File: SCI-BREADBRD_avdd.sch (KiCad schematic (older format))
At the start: 25 parts, among them P8 TP, U2 TPS62240DDC, U3 TPS73401DDC, U4 TS5A3159ADCK, U5 TS5A3159ADCK

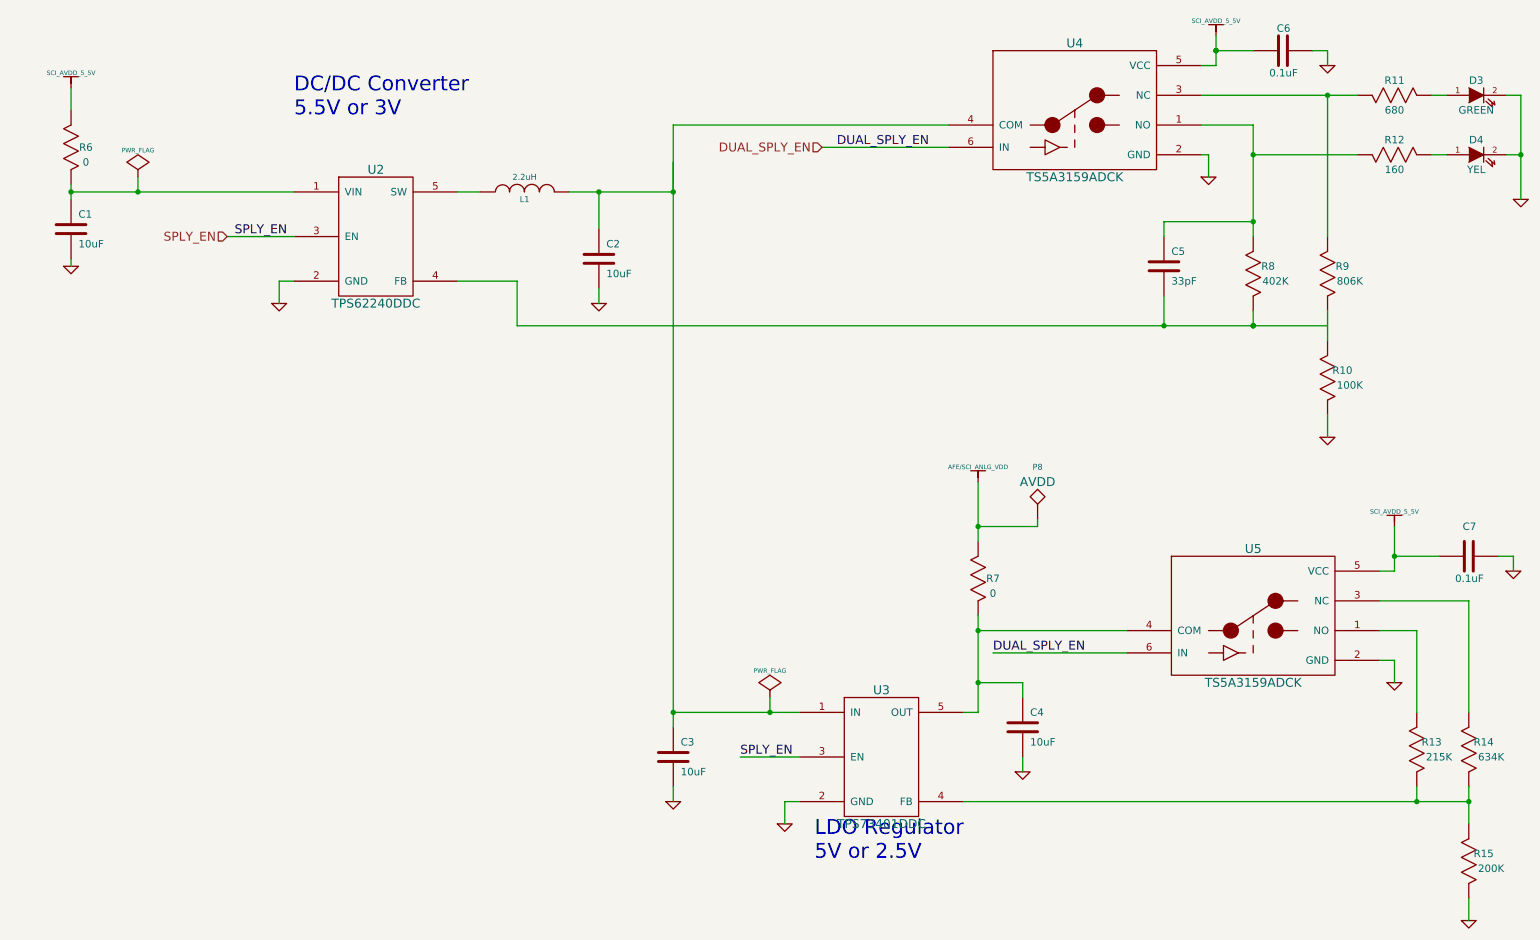
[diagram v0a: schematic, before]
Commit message: Enlarged the text on all of the power rails to make them easier to see when plotted
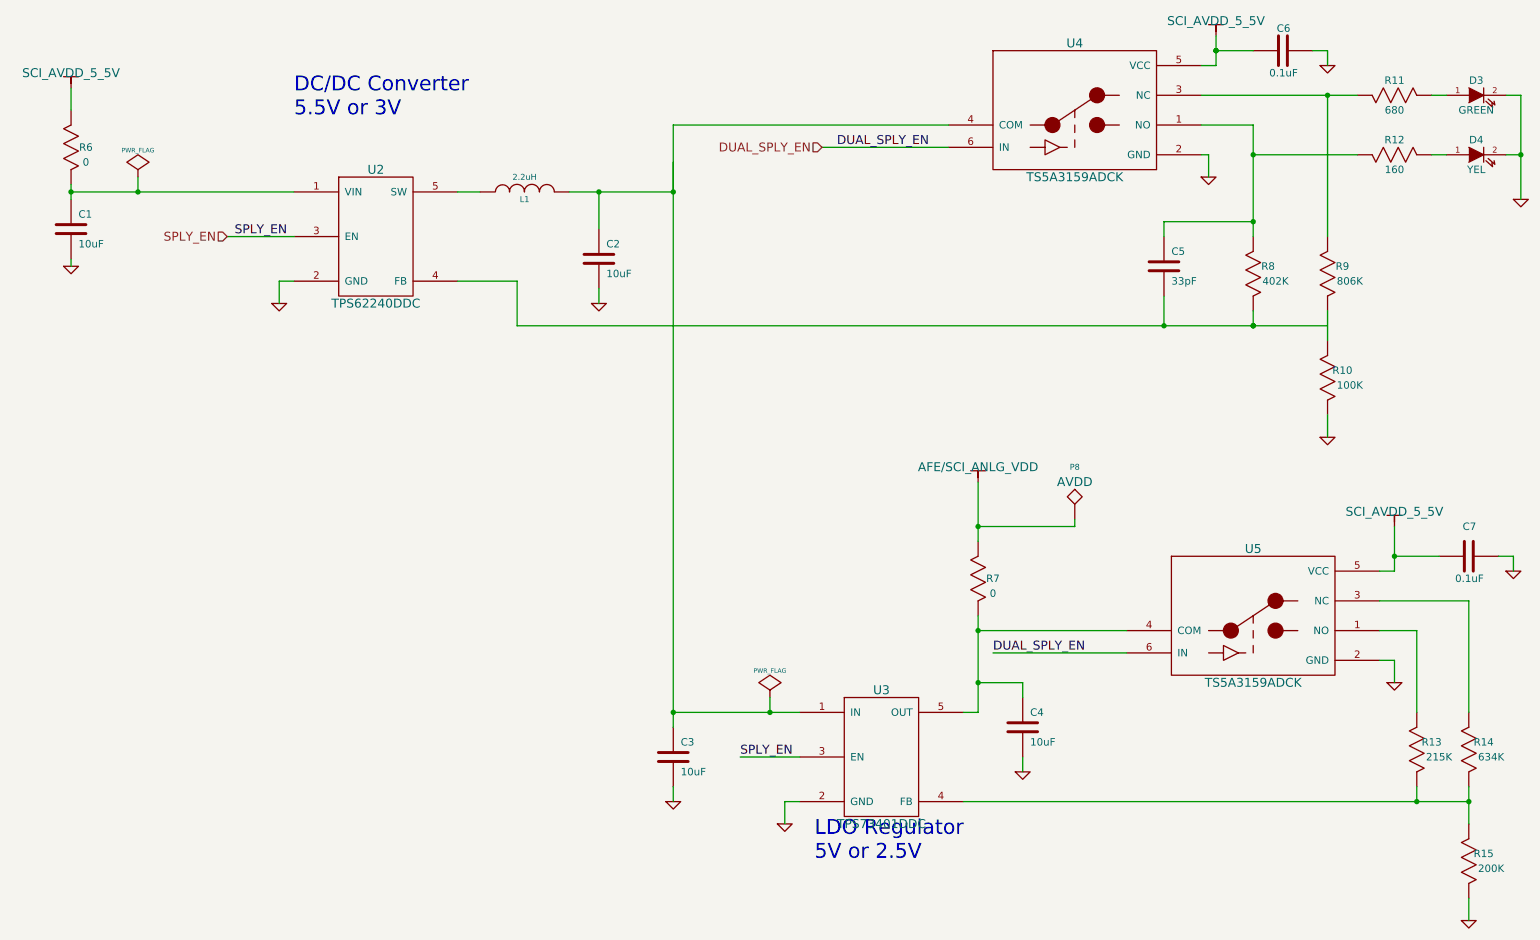
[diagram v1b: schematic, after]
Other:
- moved on the sheet: P8
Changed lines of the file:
@@
-EESchema Schematic File Version 2  date Fri 27 Apr 2012 01:46:56 PM EDT
+EESchema Schematic File Version 2  date Fri 27 Apr 2012 02:46:40 PM EDT
 LIBS:custom_transistors
 LIBS:TI_custom
@@
 $EndComp
 $Comp
-L SCI_AVDD_5_5V #PWR48
-U 1 1 4F9A30C2
-P 1000 1150
-F 0 "#PWR48" H 1000 1250 30  0001 C CNN
-F 1 "SCI_AVDD_5_5V" H 1000 1250 30  0000 C CNN
-	1    1000 1150
-	1    0    0    -1
-$EndComp
-$Comp
 L GND #PWR50
 U 1 1 4F9A30C8
@@
 $EndComp
 $Comp
-L SCI_AVDD_5_5V #PWR57
-U 1 1 4F9A3131
-P 8700 800
-F 0 "#PWR57" H 8700 900 30  0001 C CNN
-F 1 "SCI_AVDD_5_5V" H 8700 900 30  0000 C CNN
-	1    8700 800
-	1    0    0    -1
-$EndComp
-$Comp
 L C C5
 U 1 1 4F9A313A
@@
 $EndComp
 $Comp
-L SCI_AVDD_5_5V #PWR60
-U 1 1 4F9A3161
-P 9900 4100
-F 0 "#PWR60" H 9900 4200 30  0001 C CNN
-F 1 "SCI_AVDD_5_5V" H 9900 4200 30  0000 C CNN
-	1    9900 4100
-	1    0    0    -1
-$EndComp
-$Comp
 L GND #PWR61
 U 1 1 4F9A3167
@@
 	1    7100 4450
 	0    -1   -1   0
-$EndComp
-$Comp
-L AFE/SCI_ANLG_VDD #PWR54
-U 1 1 4F9A31AB
-P 7100 3800
-F 0 "#PWR54" H 7100 3900 30  0001 C CNN
-F 1 "AFE/SCI_ANLG_VDD" H 7100 3900 30  0000 C CNN
-	1    7100 3800
-	1    0    0    -1
 $EndComp
 Text Label 7200 4950 0    60   ~ 0
@@
 	1    0    0    -1
 $EndComp
+$Comp
+L TP P8
+U 1 1 4F9AD783
+P 7750 4050
+F 0 "P8" H 7750 4400 40  0000 C CNN
+F 1 "TP" H 7750 4300 30  0001 C CNN
+F 2 "TESTVIA_p30mil_h20mil" H 7750 4050 60  0001 C CNN
+F 4 "TESTPOINT VIA" H 7750 4050 60  0001 C CNN "Description"
+F 5 "NO PART. TEST PAD ONLY." H 7750 4050 60  0001 C CNN "Note"
+F 6 "AVDD" H 7750 4300 60  0000 C CNN "Silkscreen"
+	1    7750 4050
+	1    0    0    -1
+$EndComp
+$Comp
+L SCI_AVDD_5_5V #PWR?
+U 1 1 4F9AEF89
+P 1000 1150
+F 0 "#PWR?" H 1000 1250 30  0001 C CNN
+F 1 "SCI_AVDD_5_5V" H 1000 1250 60  0000 C CNN
+	1    1000 1150
+	1    0    0    -1
+$EndComp
+$Comp
+L SCI_AVDD_5_5V #PWR?
+U 1 1 4F9AEF98
+P 8700 800
+F 0 "#PWR?" H 8700 900 30  0001 C CNN
+F 1 "SCI_AVDD_5_5V" H 8700 900 60  0000 C CNN
+	1    8700 800
+	1    0    0    -1
+$EndComp
+$Comp
+L SCI_AVDD_5_5V #PWR?
+U 1 1 4F9AEFA7
+P 9900 4100
+F 0 "#PWR?" H 9900 4200 30  0001 C CNN
+F 1 "SCI_AVDD_5_5V" H 9900 4200 60  0000 C CNN
+	1    9900 4100
+	1    0    0    -1
+$EndComp
+$Comp
+L AFE/SCI_ANLG_VDD #PWR?
+U 1 1 4F9AEFC0
+P 7100 3800
+F 0 "#PWR?" H 7100 3900 30  0001 C CNN
+F 1 "AFE/SCI_ANLG_VDD" H 7100 3900 60  0000 C CNN
+	1    7100 3800
+	1    0    0    -1
+$EndComp
 Wire Wire Line
 	1000 1150 1000 1300
 Wire Wire Line
-	1000 1850 1450 1850
-Wire Wire Line
-	1450 1850 2500 1850
+	1000 1850 2500 1850
 Wire Wire Line
 	2400 2600 2400 2450
@@
 	2400 2450 2500 2450
 Wire Wire Line
-	1000 1800 1000 1850
-Wire Wire Line
-	1000 1850 1000 1900
+	1000 1800 1000 1900
 Connection ~ 1000 1850
 Wire Wire Line
@@
 	3600 1850 3750 1850
 Wire Wire Line
-	4350 1850 4550 1850
-Wire Wire Line
-	4550 1850 5050 1850
+	4350 1850 5050 1850
 Wire Wire Line
 	4550 2600 4550 2500
@@
 	8600 1400 8950 1400
 Wire Wire Line
-	8950 1400 8950 1600
-Wire Wire Line
-	8950 1600 8950 2050
-Wire Wire Line
-	8950 2050 8950 2150
+	8950 1400 8950 2150
 Wire Wire Line
 	8650 1600 8650 1750
@@
 	8650 1600 8600 1600
 Wire Wire Line
-	8600 1200 9450 1200
-Wire Wire Line
-	9450 1200 9650 1200
+	8600 1200 9650 1200
 Wire Wire Line
 	9450 2650 9450 2850
 Wire Wire Line
-	4000 2750 8350 2750
-Wire Wire Line
-	8350 2750 8950 2750
-Wire Wire Line
-	8950 2750 9450 2750
+	4000 2750 9450 2750
 Connection ~ 8950 2750
 Connection ~ 8950 2750
@@
 	4000 2450 3600 2450
 Wire Wire Line
-	8700 800  8700 900
-Wire Wire Line
-	8700 900  8700 1000
+	8700 800  8700 1000
 Wire Wire Line
 	8700 1000 8600 1000
@@
 	7100 5350 7000 5350
 Wire Wire Line
-	7100 4700 7100 4800
-Wire Wire Line
-	7100 4800 7100 5150
-Wire Wire Line
-	7100 5150 7100 5350
+	7100 4700 7100 5350
 Wire Wire Line
 	9900 5000 9800 5000
@@
 	10050 4800 9800 4800
 Wire Wire Line
-	10400 5850 10400 5950
-Wire Wire Line
-	10400 5950 10400 6100
+	10400 5850 10400 6100
 Wire Wire Line
 	10050 5850 10050 5950
 Wire Wire Line
-	7000 5950 10050 5950
-Wire Wire Line
-	10050 5950 10400 5950
+	7000 5950 10400 5950
 Connection ~ 10400 5950
 Connection ~ 10050 5950
@@
 	5050 5950 5050 5850
 Wire Wire Line
-	7100 3800 7100 4100
-Wire Wire Line
-	7100 4100 7100 4200
-Wire Wire Line
-	7100 4100 7500 4100
-Wire Wire Line
-	7500 4100 7500 4050
+	7100 3800 7100 4200
+Wire Wire Line
+	7100 4100 7750 4100
+Wire Wire Line
+	7750 4100 7750 4050
 Connection ~ 7100 4100
 Wire Wire Line
@@
 	6050 1550 6900 1550
 Wire Wire Line
-	5050 1400 5050 1850
-Wire Wire Line
-	5050 1650 5050 5350
-Wire Wire Line
-	5050 5350 5050 5450
+	5050 1850 5050 1400
+Wire Wire Line
+	5050 1650 5050 5450
 Wire Wire Line
 	4550 2100 4550 1850
 Connection ~ 4550 1850
 Wire Wire Line
-	5050 5350 5700 5350
-Wire Wire Line
-	5700 5350 5900 5350
+	5050 5350 5900 5350
 Connection ~ 5050 1850
 Connection ~ 5050 5350
@@
 Connection ~ 8950 1600
 Wire Wire Line
-	10750 1200 10750 1600
-Wire Wire Line
-	10750 1600 10750 1900
+	10750 1200 10750 1900
 Connection ~ 10750 1600
 Wire Wire Line
@@
 	10700 4300 10700 4400
 Wire Wire Line
-	9900 4100 9900 4300
-Wire Wire Line
-	9900 4300 9900 4400
+	9900 4100 9900 4400
 Wire Wire Line
 	9900 4400 9800 4400
@@
 	1450 1750 1450 1850
 Connection ~ 1450 1850
-$Comp
-L TP P8
-U 1 1 4F9AD783
-P 7500 4050
-F 0 "P8" H 7500 4400 40  0000 C CNN
-F 1 "TP" H 7500 4300 30  0001 C CNN
-F 2 "TESTVIA_p30mil_h20mil" H 7500 4050 60  0001 C CNN
-F 4 "TESTPOINT VIA" H 7500 4050 60  0001 C CNN "Description"
-F 5 "NO PART. TEST PAD ONLY." H 7500 4050 60  0001 C CNN "Note"
-F 6 "AVDD" H 7500 4300 60  0000 C CNN "Silkscreen"
-	1    7500 4050
-	1    0    0    -1
-$EndComp
 $EndSCHEMATC

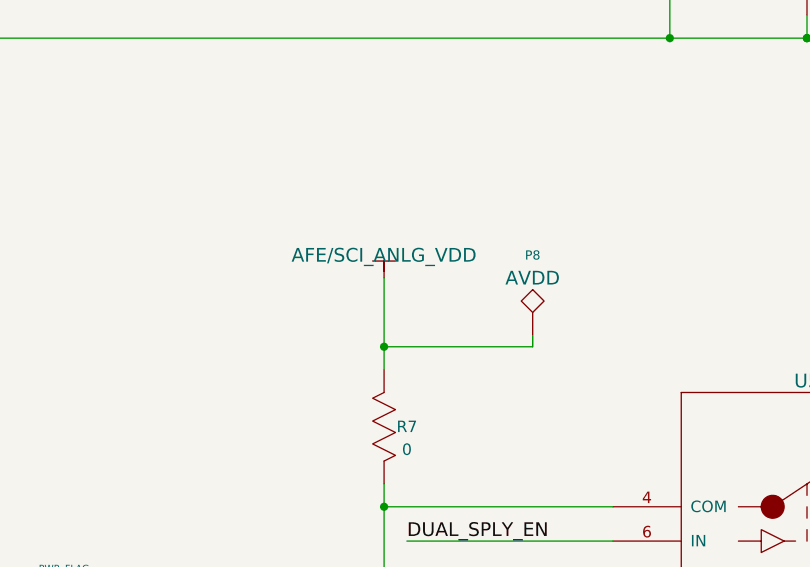
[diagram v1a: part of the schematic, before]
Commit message: No longer connecting the power circuitry directly to AFE/SCI_ANLG power rails.
This is just too dangerous with AFE modules that also generate power
on those rails. For this board, the user can manually jumper the
circuitry to the rails as desired.
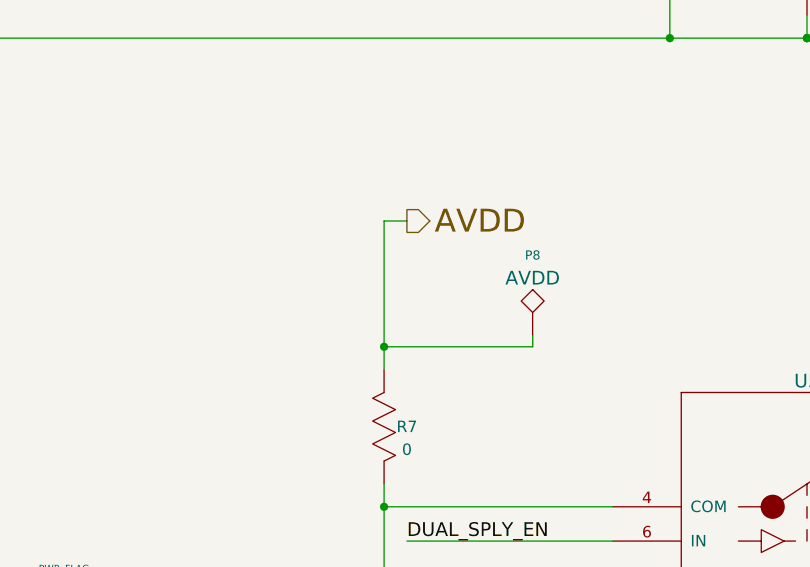
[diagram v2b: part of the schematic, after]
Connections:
- net AFE/SCI_ANLG_VDD renamed AVDD
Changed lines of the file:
@@
-EESchema Schematic File Version 2  date Fri 27 Apr 2012 02:46:40 PM EDT
+EESchema Schematic File Version 2  date Tue 01 May 2012 11:50:12 PM EDT
 LIBS:custom_transistors
 LIBS:TI_custom
@@
 Sheet 7 9
 Title "SCI-BREADBRD-MVK"
-Date "27 apr 2012"
+Date "2 may 2012"
 Rev "A"
 Comp "The Ohio State University"
@@
 $EndComp
 $Comp
+L SCI_AVDD_5_5V #PWR?
+U 1 1 4F9AEF89
+P 1000 1150
+F 0 "#PWR?" H 1000 1250 30  0001 C CNN
+F 1 "SCI_AVDD_5_5V" H 1000 1250 60  0000 C CNN
+	1    1000 1150
+	1    0    0    -1
+$EndComp
+$Comp
+L SCI_AVDD_5_5V #PWR?
+U 1 1 4F9AEF98
+P 8700 800
+F 0 "#PWR?" H 8700 900 30  0001 C CNN
+F 1 "SCI_AVDD_5_5V" H 8700 900 60  0000 C CNN
+	1    8700 800
+	1    0    0    -1
+$EndComp
+$Comp
+L SCI_AVDD_5_5V #PWR?
+U 1 1 4F9AEFA7
+P 9900 4100
+F 0 "#PWR?" H 9900 4200 30  0001 C CNN
+F 1 "SCI_AVDD_5_5V" H 9900 4200 60  0000 C CNN
+	1    9900 4100
+	1    0    0    -1
+$EndComp
+$Comp
 L TP P8
 U 1 1 4F9AD783
@@
 	1    0    0    -1
 $EndComp
-$Comp
-L SCI_AVDD_5_5V #PWR?
-U 1 1 4F9AEF89
-P 1000 1150
-F 0 "#PWR?" H 1000 1250 30  0001 C CNN
-F 1 "SCI_AVDD_5_5V" H 1000 1250 60  0000 C CNN
-	1    1000 1150
-	1    0    0    -1
-$EndComp
-$Comp
-L SCI_AVDD_5_5V #PWR?
-U 1 1 4F9AEF98
-P 8700 800
-F 0 "#PWR?" H 8700 900 30  0001 C CNN
-F 1 "SCI_AVDD_5_5V" H 8700 900 60  0000 C CNN
-	1    8700 800
-	1    0    0    -1
-$EndComp
-$Comp
-L SCI_AVDD_5_5V #PWR?
-U 1 1 4F9AEFA7
-P 9900 4100
-F 0 "#PWR?" H 9900 4200 30  0001 C CNN
-F 1 "SCI_AVDD_5_5V" H 9900 4200 60  0000 C CNN
-	1    9900 4100
-	1    0    0    -1
-$EndComp
-$Comp
-L AFE/SCI_ANLG_VDD #PWR?
-U 1 1 4F9AEFC0
-P 7100 3800
-F 0 "#PWR?" H 7100 3900 30  0001 C CNN
-F 1 "AFE/SCI_ANLG_VDD" H 7100 3900 60  0000 C CNN
-	1    7100 3800
-	1    0    0    -1
-$EndComp
+Text HLabel 7200 3550 2    100  Output ~ 0
+AVDD
 Wire Wire Line
 	1000 1150 1000 1300
@@
 	5050 5950 5050 5850
 Wire Wire Line
-	7100 3800 7100 4200
+	7100 3550 7100 4200
 Wire Wire Line
 	7100 4100 7750 4100
@@
 	1450 1750 1450 1850
 Connection ~ 1450 1850
+Wire Wire Line
+	7100 3550 7200 3550
 $EndSCHEMATC

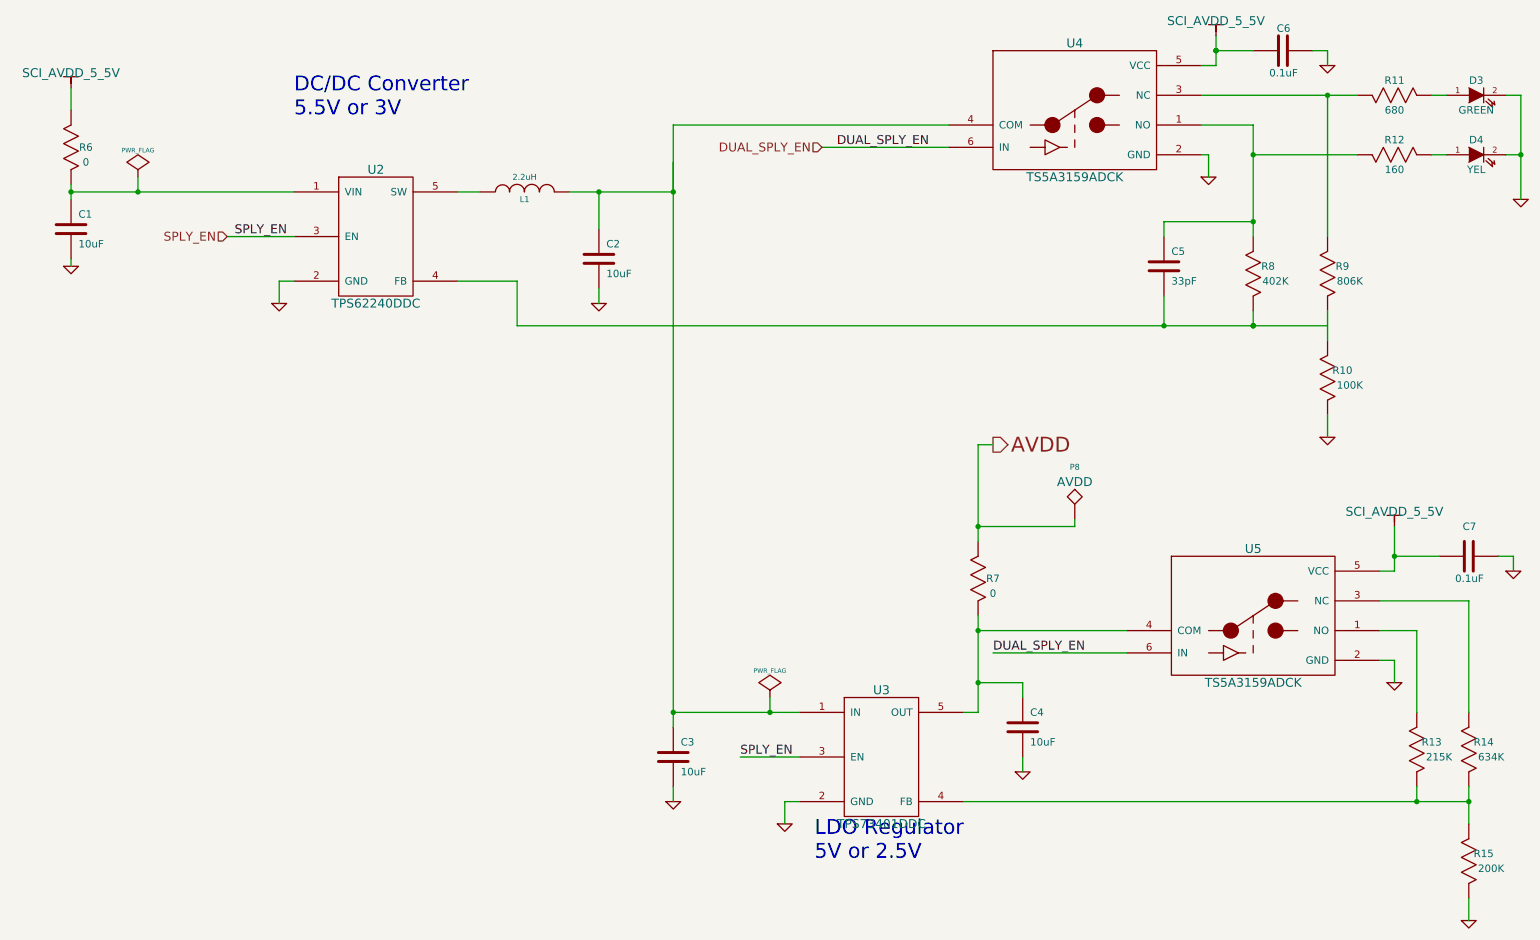
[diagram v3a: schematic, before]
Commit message: Added some bypass caps. Rearranged pins on connectors to make layout easier.
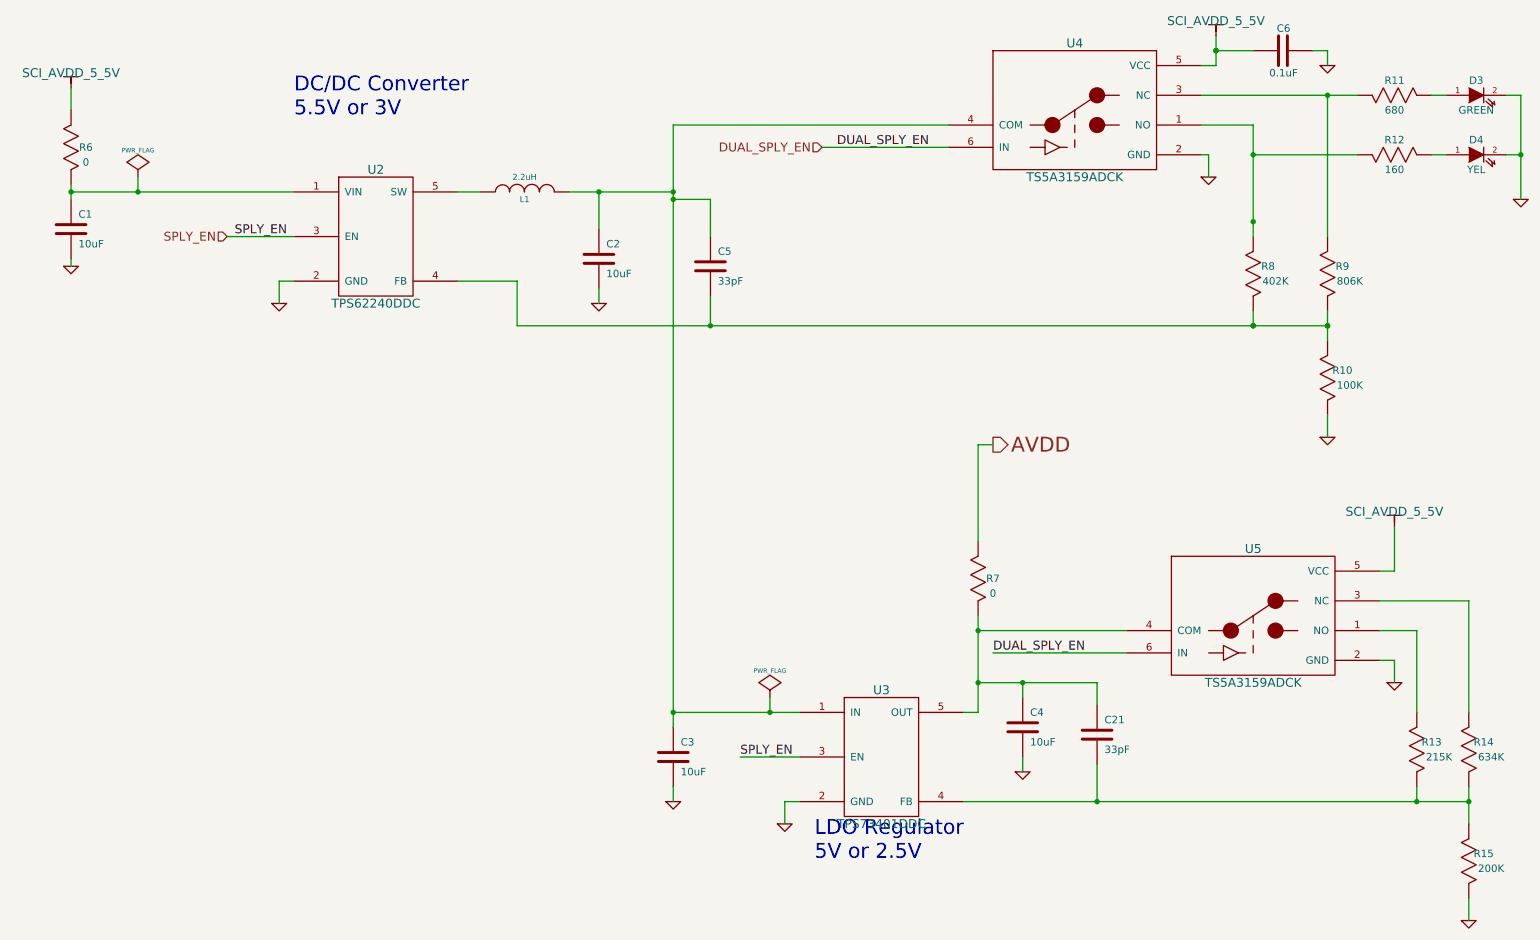
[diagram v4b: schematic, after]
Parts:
- removed C7: 0.1uF, 0402, symbol C
- removed P8: TP, TESTVIA_p30mil_h20mil, symbol TP
- added C21: 33pF, 0402, symbol C
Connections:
- net at C2.1, C3.1, L1.2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: now also C5.1
- net at C5.2, R8.1 (A), U2.4 (FB): now also R10.2 (B), R9.1 (A)
- net at R13.1 (A), R14.1 (A), R15.2 (B)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: now also C21.2
- net at C4.1, R7.1 (A), U3.5 (OUT)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: now also C21.1
- net at R12.1 (A), R8.2 (B), U4.1 (NO): no longer C5.1
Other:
- moved on the sheet: C5
